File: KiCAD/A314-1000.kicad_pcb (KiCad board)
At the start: 4 copper layers, 163.4 x 59.5 mm, 93 parts, among them IC1 T8Q144xx, IC2 SN74CBTD3384CPWR, IC3 SN74CBTD3384CPWR, IC4 SN74CBTD3384CPWR, IC5 SN74CBTD3384CPWR, IC6 IS61WV12816EDBLL-10TLI, IC7 LM1117MP-1.2, IC8 LM1117MP-3.3, J1 Raspberry_Pi_2_3, J2 2x30 Card edge conn.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

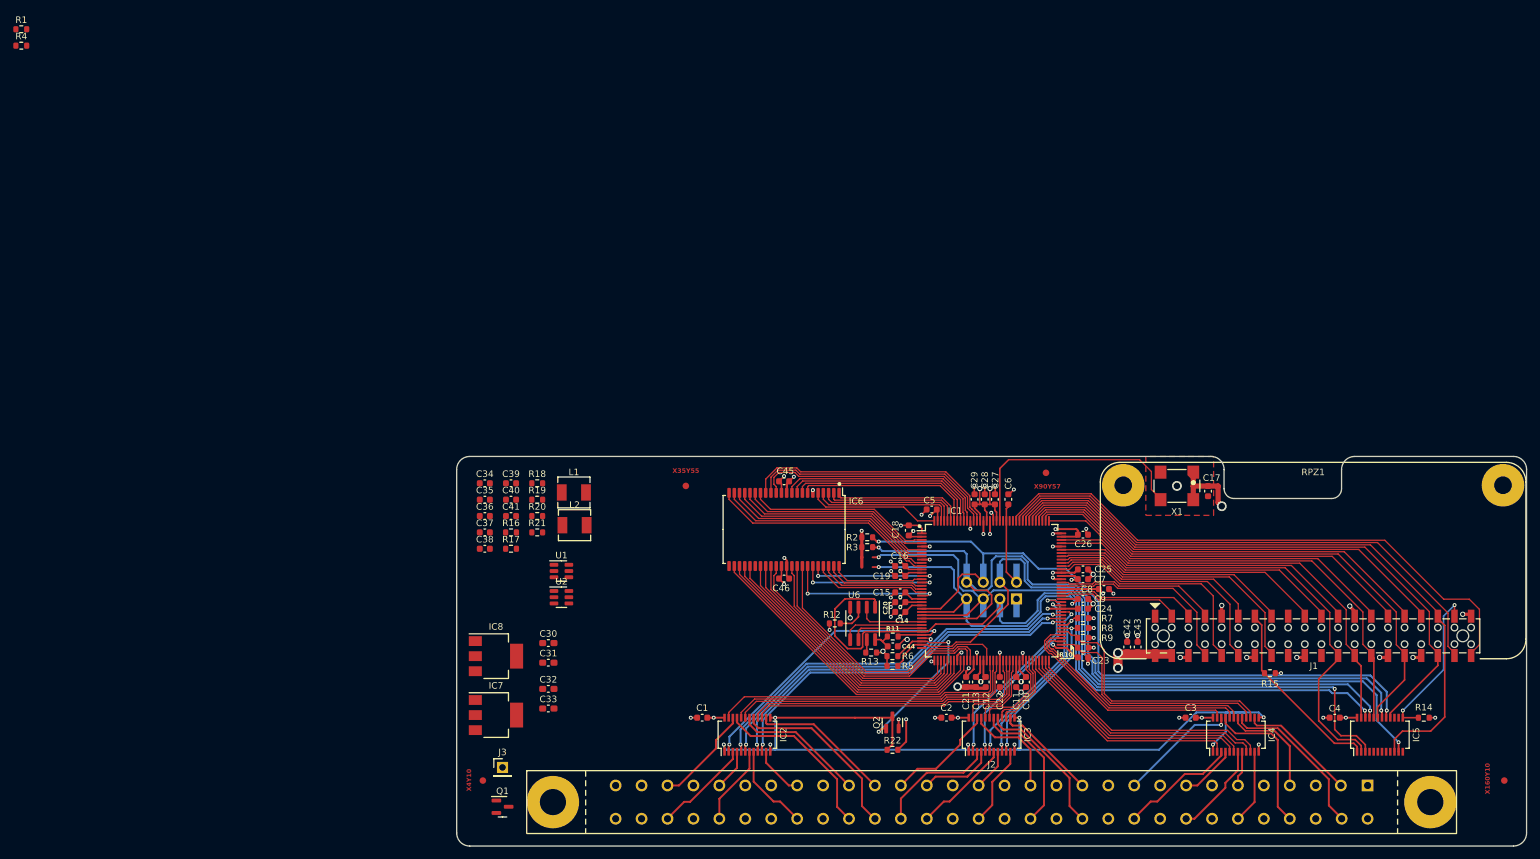
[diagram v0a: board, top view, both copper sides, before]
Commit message: Ready for production?
Board finished, added a RTC for the RPi. With a little luck and some production files, this may be ready for some PCBA :)
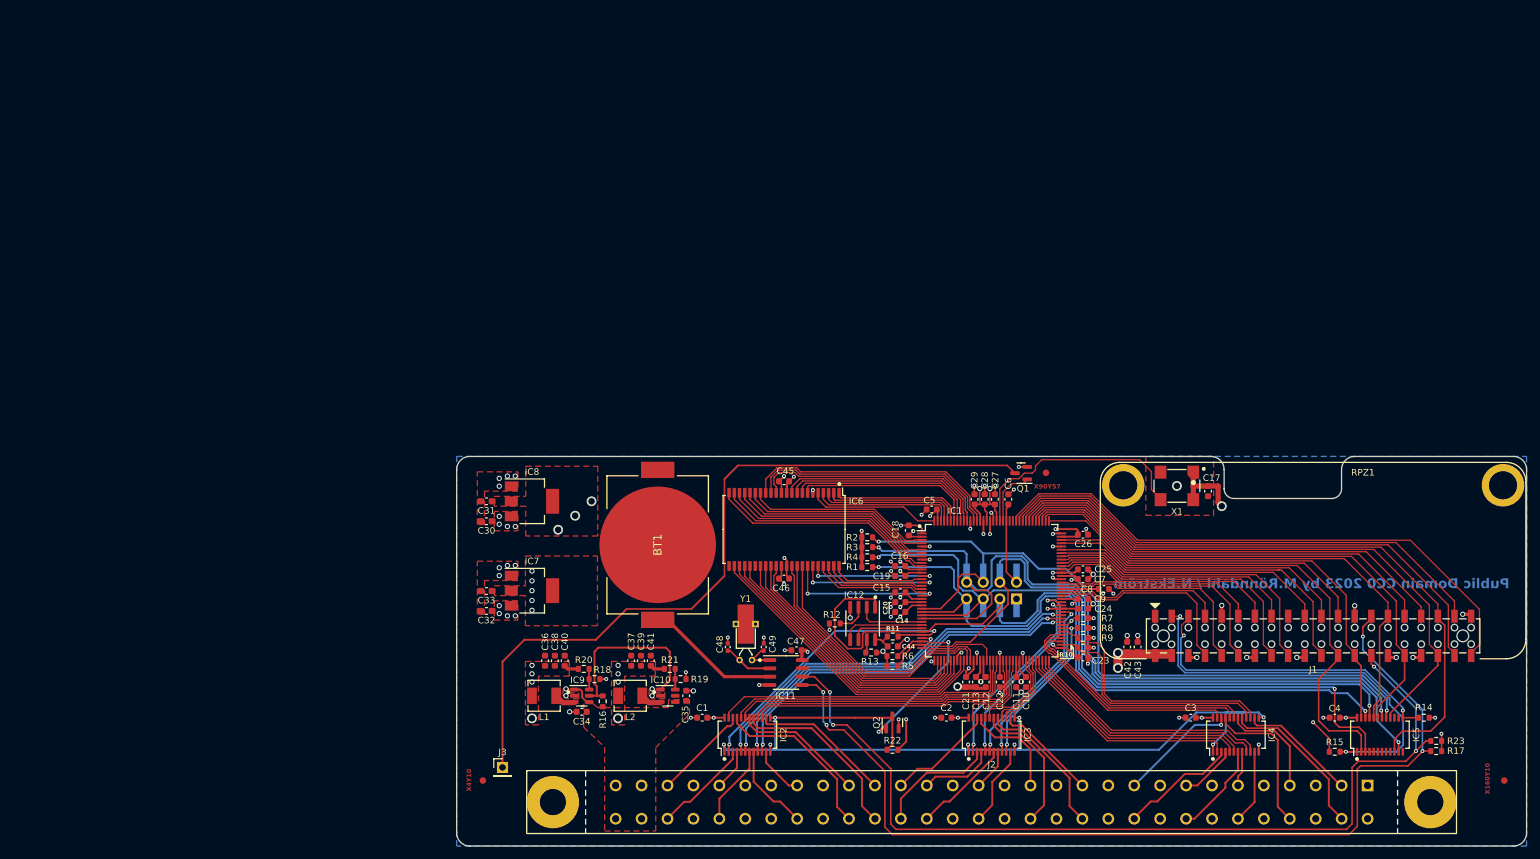
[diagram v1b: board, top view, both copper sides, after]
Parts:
- removed the REF** at (161.3, 69.1)
- removed the REF** at (98.5, 70.1)
- removed the REF** at (71.5, 115.4)
- removed the REF** at (228.0, 115.5)
- added BT1: CR2032, A314-1000:BATHLD001, F.Cu at (98.7, 79.5)
- added C47: 100n, Capacitor_SMD:C_0603_1608Metric, F.Cu at (119.9, 95.6)
- added C48: 8p, Capacitor_SMD:C_0402_1005Metric_Pad0.74x0.62mm_HandSolder, F.Cu at (109.4, 95.1)
- added C49: 8p, Capacitor_SMD:C_0402_1005Metric_Pad0.74x0.62mm_HandSolder, F.Cu at (114.9, 95.1)
- added FID1: Fiducial, Fiducial:Fiducial_1mm_Mask2mm, F.Cu at (72.0, 115.5)
- added FID2: Fiducial, Fiducial:Fiducial_1mm_Mask2mm, F.Cu at (158.0, 68.5)
- added FID3: Fiducial, Fiducial:Fiducial_1mm_Mask2mm, F.Cu at (228.0, 115.5)
- added IC11: PT7C4311WEX, Package_SO:SOIC-8_3.9x4.9mm_P1.27mm, F.Cu at (118.3, 99.0)
- added R23: 3k9, Resistor_SMD:R_0603_1608Metric, F.Cu at (217.6, 109.5)
- added REF**: OSHW-Logo2_14.6x12mm_SilkScreen, Symbol:OSHW-Logo2_14.6x12mm_SilkScreen, B.Cu at (99.8, 79.0)
- added Y1: 32.768kHz, Crystal:Crystal_DS26_D2.0mm_L6.0mm_Horizontal_1EP_style2, F.Cu at (113.1, 97.1)
- J3: value Conn_01x01 -> INT2
- R17: value 442k -> 3k9
- moved R1 153.1 mm to (130.7, 82.9), turned to 180 degrees
- moved R4 151.0 mm to (130.7, 81.4), turned to 180 degrees
- moved R17 144.6 mm to (217.6, 111.0)
- moved Q1 94.2 mm to (154.2, 68.5), turned to 180 degrees
- moved C35 42.9 mm to (103.0, 102.5), turned to 90 degrees
- moved C34 37.9 mm to (87.1, 105.0), turned to 180 degrees
- moved R19 35.1 mm to (102.2, 100.0), turned to 180 degrees
- moved C39 33.6 mm to (96.2, 97.2), turned to 90 degrees
- moved L1 31.4 mm to (81.3, 102.5), turned to 180 degrees
- moved R18 31.2 mm to (89.0, 100.0), turned to 180 degrees
- moved C41 30.7 mm to (97.7, 97.2), turned to 90 degrees
- moved C37 29.7 mm to (94.7, 97.2), turned to 90 degrees
- moved R16 29.4 mm to (90.3, 103.4), turned to -90 degrees
- moved R21 29.1 mm to (100.5, 98.5), turned to 180 degrees
- moved L2 27.4 mm to (94.5, 102.5), turned to 180 degrees
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- renumbered U2 to IC10, U6 to IC12, U1 to IC9
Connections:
- net Net-(U1-PG) renamed /1V2PG
- IC1 pad 100: /PIIRQ -> /PIACK
- IC1 pad 101: /PIACK -> /PIA_{0}
- IC1 pad 103: /PID_{5} -> /PIA_{1}
- IC1 pad 105: /PID_{4} -> /PID_{5}
- IC1 pad 106: /PID_{7} -> /PID_{4}
- IC1 pad 109: /PID_{3} -> /PID_{7}
- IC1 pad 110: /PIA_{1} -> /PID_{3}
- IC1 pad 111: /PIA_{0} -> /PID_{1}
- IC1 pad 112: /PID_{1} -> /PID_{8}
- IC1 pad 113: /PID_{8} -> /PID_{2}
- IC1 pad 114: /PID_{2} -> /PID_{9}
- IC1 pad 115: /PID_{9} -> /PID_{12}
- IC1 pad 116: /PID_{12} -> /PID_{15}
- IC1 pad 117: /PID_{15} -> /PIWR
- IC1 pad 118: /PIWR -> /PIA_{2}
- IC1 pad 123: unconnected-(IC1D-GPIOR_77/PLLIN1-Pad123) -> Net-(IC1D-GPIOR_77/PLLIN1)
- IC1 pad 24: +3V3 -> /TDO
- IC1 pad 89: /PIA_{2} -> /PID_{10}
- IC1 pad 90: /PIA_{3} -> /PID_{0}
- IC1 pad 92: /PID_{10} -> /PID_{11}
- IC1 pad 93: /PID_{0} -> /PID_{14}
- IC1 pad 97: /PID_{11} -> /PID_{13}
- IC1 pad 98: /PID_{14} -> /PIA_{3}
- IC1 pad 99: /PID_{13} -> /PIIRQ
- IC10 pad 5: Net-(U2-PG) -> unconnected-(IC10-PG-Pad5)
- IC5 pad 17: +3V3 -> /TDO
- IC5 pad 20: /PIA_{1} -> /PID_{1}
- J1 pad 13: /JTAG_OE_{1} -> /PIA_{3}
- J1 pad 18: unconnected-(J1-GPIO24-Pad18) -> /PIA_{0}
- J1 pad 22: unconnected-(J1-GPIO25-Pad22) -> /PIA_{1}
- J1 pad 27: /PIA_{0} -> Net-(IC11-SDA)
- J1 pad 28: /PIA_{1} -> Net-(IC11-SCL)
- J1 pad 3: /PIA_{2} -> /JTAG_OE_{1}
- J1 pad 37: /JTAG_OE_{0} -> /PIA_{2}
- J1 pad 5: /PIA_{3} -> /JTAG_OE_{0}
- J4 pad 6: +3V3 -> /TDO
- Q1 pad 1: INT2 -> Net-(IC1D-GPIOR_77/PLLIN1)
- R17 pad 1: Net-(U2-PG) -> Net-(IC11-SDA)
- R17 pad 2: +5V -> +3V3
- R2 pad 1: +3V3 -> /TDO
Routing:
- net Net-(IC11-SDA): track 0.00 -> 149.3 mm, vias 0 -> 4
- net Net-(IC11-SCL): track 0.00 -> 142.2 mm, vias 0 -> 4
- net Net-(J3-Pin_1): track 0.00 -> 116.0 mm
- net /TDO: track 0.00 -> 115.5 mm
- net +3V3: track 217.7 -> 113.6 mm, vias 22 -> 31
- net /PIA_{2}: track 18.7 -> 77.4 mm
- net /JTAG_OE_{1}: track 28.9 -> 63.8 mm, vias 0 -> 2
- net /1V2PG: track 0.00 -> 27.4 mm
- net /JTAG_OE_{0}: track 24.6 -> 49.3 mm
- net /PIA_{1}: track 72.3 -> 51.3 mm
- net Net-(BT1-+): track 0.00 -> 20.7 mm
- net /PID_{1}: track 61.5 -> 78.0 mm
- net /PIA_{3}: track 21.3 -> 34.7 mm
- net /PIA_{0}: track 58.1 -> 45.8 mm
- net GND: track 81.4 -> 91.1 mm, vias 56 -> 77
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- added copper zone on F.Cu, net +1V2
- added copper zone on F.Cu, net +3V3
- added copper zone on F.Cu, net +5V
- added copper zone on B.Cu, net GND
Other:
- board text added: "A314-1000"
- board text added: "Public Domain CC0 2023 by M.Rönndahl / N.Ekström"
- board text removed: "X35Y55"

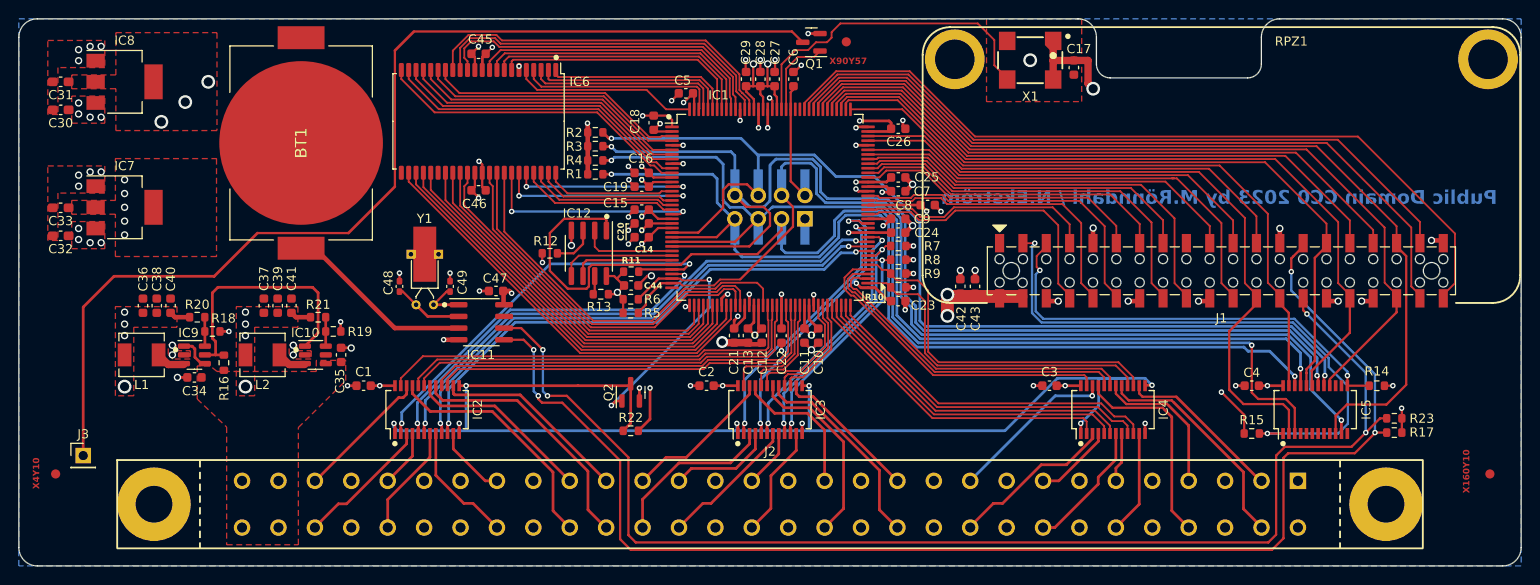
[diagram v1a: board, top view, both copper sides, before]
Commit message: Simplified PSU
Enhanced battery replacement ergonomics
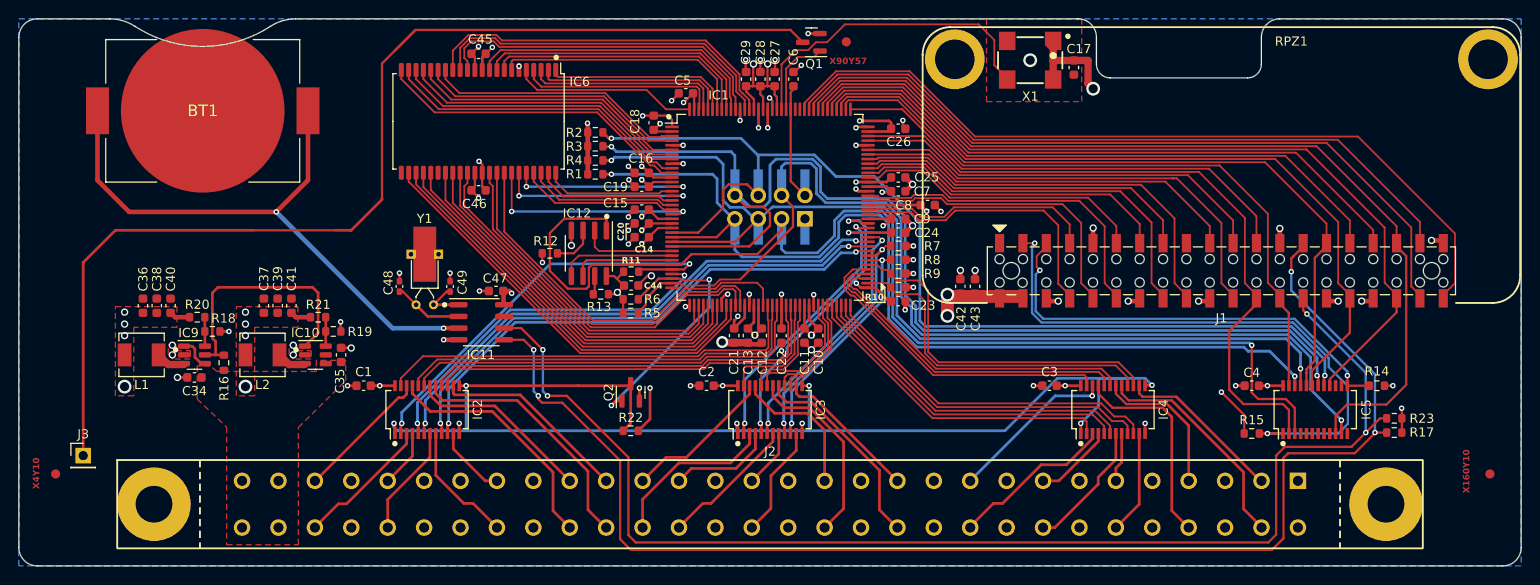
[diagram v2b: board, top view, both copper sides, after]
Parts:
- removed C30, C31, C32, C33: 10u, Capacitor_SMD:C_0603_1608Metric_Pad1.08x0.95mm_HandSolder
- removed IC7: LM1117MP-1.2, Package_TO_SOT_SMD:SOT-223-3_TabPin2
- removed IC8: LM1117MP-3.3, Package_TO_SOT_SMD:SOT-223-3_TabPin2
- moved REF** 18.4 mm to (86.2, 91.3)
- moved BT1 11.3 mm to (88.0, 76.0), turned to 180 degrees
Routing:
- net Net-(BT1-+): track 20.7 -> 65.9 mm, vias 0 -> 2
- net Net-(J3-Pin_1): track 116.0 -> 119.0 mm
- net GND: vias 77 -> 69
- net +5V: vias 14 -> 6
- net +3V3: vias 31 -> 28
- net +1V2: vias 20 -> 15
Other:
- outline, holes or cut-outs redrawn
- board text added: "CR2032"

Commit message: General cleanup
Removed irrelevant files, addressed a number of DRC issues and cleaned up a footprint or two :)
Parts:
- moved IC12 0.10 mm to (130.0, 91.6)
- moved J3 0.10 mm to (75.0, 113.4)
- moved R13 0.10 mm to (131.3, 96.0)
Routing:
- net +1V2: track 54.4 -> 68.1 mm
- net GND: track 91.1 -> 104.5 mm, vias 69 -> 82
- net /3VA_{4}: track 36.3 -> 31.6 mm
- net /TCK: track 109.3 -> 108.3 mm
- net Net-(IC11-SCL): track 142.2 -> 141.3 mm
- net /TDO: track 115.5 -> 116.4 mm
- net +3V3: track 113.6 -> 114.5 mm, vias 28 -> 29
- net /PIA_{1}: track 51.3 -> 50.5 mm
- net /PID_{9}: track 69.3 -> 68.6 mm
- net /JTAG_OE_{1}: track 63.8 -> 63.1 mm
- net Net-(IC11-SDA): track 149.3 -> 148.7 mm
- net /PIACK: track 38.0 -> 37.4 mm
- net /JTAG_OE_{0}: track 49.3 -> 48.7 mm

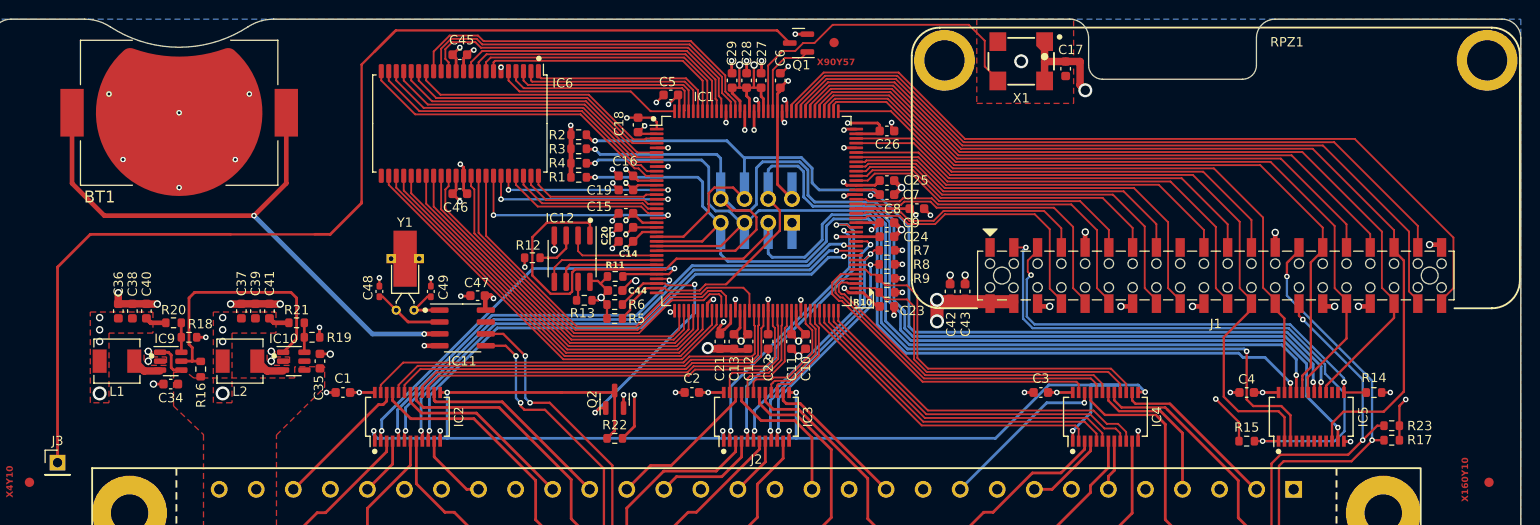
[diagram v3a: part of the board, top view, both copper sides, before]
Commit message: First bug-ridded release
This is the first non-alpha release. The hardware issues that were found in the alpha have been addressed. This board is now sent for a second production run.
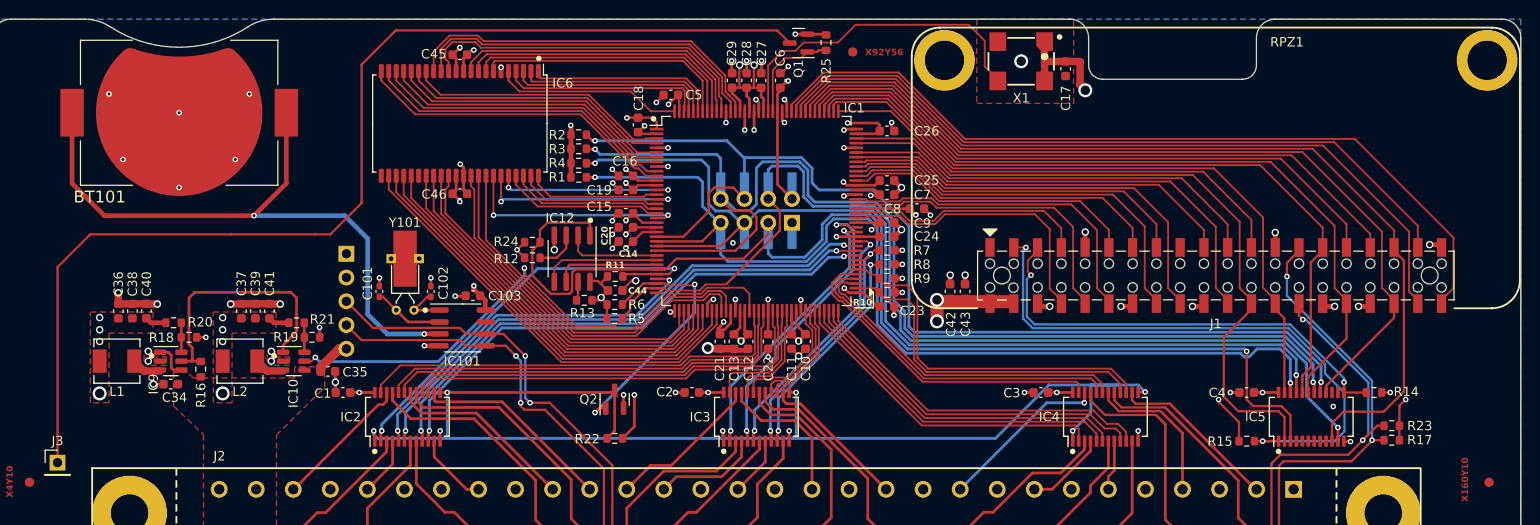
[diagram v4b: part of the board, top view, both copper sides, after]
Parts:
- removed REF**: OSHW-Logo2_14.6x12mm_SilkScreen, Symbol:OSHW-Logo2_14.6x12mm_SilkScreen
- added H1: MountingHole, A314-1000:M2.5_Mount, F.Cu at (169.8, 70.4)
- added H2: MountingHole, A314-1000:M2.5_Mount, F.Cu at (227.8, 70.4)
- added J5: RASP_I2C, Connector_PinHeader_2.54mm:PinHeader_1x05_P2.54mm_Vertical, B.Cu at (105.9, 91.1)
- added R24: 10k, Resistor_SMD:R_0603_1608Metric, F.Cu at (125.7, 89.8)
- added R25: 3k9, Resistor_SMD:R_0603_1608Metric, F.Cu at (157.1, 68.5)
- R1: value 6 x 10k -> 10k
- R7: value 4 x 10k -> 10k
- moved C35 1.39 mm to (103.9, 103.7), turned to 0 degrees
- moved C103 0.50 mm to (119.4, 95.5)
- renumbered BT1 to BT101, C48 to C101, C49 to C102, C47 to C103, IC11 to IC101, Y1 to Y101
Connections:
- net Net-(IC11-SCL) renamed /SCL
- net Net-(IC11-SDA) renamed /SDA
- IC10 pad 5: unconnected-(IC10-PG-Pad5) -> /~{CRESET}
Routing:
- net /~{CRESET}: track 112.2 -> 154.6 mm, vias 1 -> 3
- net /SCL: track 141.3 -> 158.3 mm
- net /SDA: track 148.7 -> 164.5 mm
- net Net-(BT101-+): track 65.9 -> 70.7 mm
- net +5V: track 30.9 -> 34.9 mm
- net GND: track 104.5 -> 106.8 mm, vias 82 -> 83
- net /TMS: track 107.4 -> 109.6 mm
- net Net-(IC1D-GPIOR_77/PLLIN1): track 8.90 -> 11.0 mm
- net +3V3: track 114.5 -> 116.2 mm
- net /A_{11}: track 46.8 -> 47.3 mm
- net /D_{8}: track 40.6 -> 41.1 mm
- net /A_{9}: track 43.7 -> 44.3 mm
- net /A_{10}: track 45.3 -> 45.9 mm
- net /A_{8}: track 42.3 -> 42.9 mm
- net /D_{9}: track 39.2 -> 39.7 mm
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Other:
- board text added: "GND +3V3 SCL SDA +5V"
- board text added: "X92Y56"
- board text removed: "X90Y57"
